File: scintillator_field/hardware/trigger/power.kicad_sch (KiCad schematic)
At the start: 16 parts, among them U2 TPS7A4701, U4 TPS7A4701, U5 LT3461A

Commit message: conclude schematic
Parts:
- added R10: 12k 0.1%, symbol Device:R
- added R9: 10k 0.1%, symbol Device:R
- C1: renamed from C16; footprint (none) -> Capacitor_SMD:C_0402_1005Metric
- C2: renamed from C17; footprint (none) -> Capacitor_SMD:C_0402_1005Metric
- C3: renamed from C15; footprint (none) -> Capacitor_SMD:C_0402_1005Metric
- C4: renamed from C1; footprint (none) -> Capacitor_SMD:C_0402_1005Metric
- C5: renamed from C18; value 47u -> 10u; footprint (none) -> Capacitor_SMD:C_1206_3216Metric
- C6: renamed from C19; footprint (none) -> Capacitor_SMD:C_0402_1005Metric
- C7: renamed from C20; value 47u -> 10u; footprint (none) -> Capacitor_SMD:C_1206_3216Metric
- C8: renamed from C14; footprint (none) -> Capacitor_SMD:C_0402_1005Metric
- renumbered R4 to R5, R2 to R6, R6 to R7, R7 to R8, U5 to U1, U4 to U3
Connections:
- net +3.8V: now also R9.1
- net GND: now also R10.1
- new net +2.1V: R10.2, R9.2
- no-connect marks 0 -> 14
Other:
- moved on the sheet: C1, C2, C3, C4, C5, C6, C7, C8, L1, R5, R6, R7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

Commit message: pcb v1
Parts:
- added C45: 1u, Capacitor_SMD:C_0402_1005Metric, symbol Device:C
- added C46: 0.1u, Capacitor_SMD:C_0402_1005Metric, symbol Device:C
- L1: footprint (none) -> lqh3npn:L_Murata_LQH3NPN_3.0x3.0mm
- R10, R5: footprint (none) -> Resistor_SMD:R_0402_1005Metric
- R6, R7, R8, R9: footprint (none) -> Resistor_SMD:R_0603_1608Metric
- U2, U3: symbol Regulator_Linear:TPS7A4701xRGW -> tps7a4701:TPS7A4701xRGW
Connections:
- net +5V: now also C45.1, C46.1
- net GND: now also U2.17 (NC), U2.18 (NC), U2.19 (NC), U2.2 (NC), U3.17 (NC), U3.18 (NC), U3.19 (NC), U3.2 (NC), C45.2, C46.2
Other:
- moved on the sheet: C1, C2, C7, L1, R5, R6, R7, R8, U1

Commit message: pcb fabrication files
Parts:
- C1: LCSC (none) -> C88923
- C2, C3, C4, C45, C6, C8: LCSC (none) -> C52923
- C46: LCSC (none) -> C1581
- C5, C7: LCSC (none) -> C13585
- L1: LCSC (none) -> C237408
- R10, R5: LCSC (none) -> C317927
- R6: LCSC (none) -> C861317
- R7: LCSC (none) -> C861233
- R8, R9: LCSC (none) -> C136139
- U1: LCSC (none) -> C481768
- U2, U3: LCSC (none) -> C90084
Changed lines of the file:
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@@
+			)
+		)
+		(property "LCSC" "C136139"
+			(at 149.86 99.06 0)
+			(effects
+				(font
+					(size 1.27 1.27)
+				)
+				(hide yes)
 			)
 		)
@@
 			)
 		)
+		(property "LCSC" "C88923"
+			(at 52.07 116.84 0)
+			(effects
+				(font
+					(size 1.27 1.27)
+				)
+				(hide yes)
+			)
+		)
 		(pin "2"
 		)
@@
 			)
 		)
+		(property "LCSC" "C481768"
+			(at 52.07 96.52 0)
+			(effects
+				(font
+					(size 1.27 1.27)
+				)
+				(hide yes)
+			)
+		)
 		(pin "1"
 		)
@@
 			)
 		)
+		(property "LCSC" "C317927"
+			(at 35.56 111.76 0)
+			(effects
+				(font
+					(size 1.27 1.27)
+				)
+				(hide yes)
+			)
+		)
 		(pin "2"
 		)
@@
 			)
 		)
+		(property "LCSC" "C52923"
+			(at 217.17 114.3 0)
+			(effects
+				(font
+					(size 1.27 1.27)
+				)
+				(hide yes)
+			)
+		)
 		(pin "2"
 		)
@@
 			)
 		)
+		(property "LCSC" "C317927"
+			(at 243.84 107.95 0)
+			(effects
+				(font
+					(size 1.27 1.27)
+				)
+				(hide yes)
+			)
+		)
 		(pin "2"
 		)
@@
 			)
 		)
+		(property "LCSC" "C237408"
+			(at 52.07 80.01 0)
+			(effects
+				(font
+					(size 1.27 1.27)
+				)
+				(hide yes)
+			)
+		)
 		(pin "1"
 		)
@@
 			)
 		)
+		(property "LCSC" "C1581"
+			(at 71.12 107.95 0)
+			(effects
+				(font
+					(size 1.27 1.27)
+				)
+				(hide yes)
+			)
+		)
 		(pin "2"
 		)
@@
 		)
 		(property "Description" "Unpolarized capacitor"
+			(at 76.2 107.95 0)
+			(effects
+				(font
+					(size 1.27 1.27)
+				)
+				(hide yes)
+			)
+		)
+		(property "LCSC" "C52923"
 			(at 76.2 107.95 0)
 			(effects
@@
 			)
 		)
+		(property "LCSC" "C52923"
+			(at 110.49 88.9 0)
+			(effects
+				(font
+					(size 1.27 1.27)
+				)
+				(hide yes)
+			)
+		)
 		(pin "2"
 		)
@@
 			)
 		)
+		(property "LCSC" "C90084"
+			(at 203.2 99.06 0)
+			(effects
+				(font
+					(size 1.27 1.27)
+				)
+				(hide yes)
+			)
+		)
 		(pin "5"
 		)
@@
 			)
 		)
+		(property "LCSC" "C136139"
+			(at 243.84 87.63 0)
+			(effects
+				(font
+					(size 1.27 1.27)
+				)
+				(hide yes)
+			)
+		)
 		(pin "1"
 		)
@@
 		)
 		(property "Description" "Unpolarized capacitor"
+			(at 139.7 114.3 0)
+			(effects
+				(font
+					(size 1.27 1.27)
+				)
+				(hide yes)
+			)
+		)
+		(property "LCSC" "C52923"
 			(at 139.7 114.3 0)
 			(effects
@@
 			)
 		)
+		(property "LCSC" "C52923"
+			(at 186.69 90.17 0)
+			(effects
+				(font
+					(size 1.27 1.27)
+				)
+				(hide yes)
+			)
+		)
 		(pin "2"
 		)
@@
 			)
 		)
+		(property "LCSC" "C13585"
+			(at 163.83 93.98 0)
+			(effects
+				(font
+					(size 1.27 1.27)
+				)
+				(hide yes)
+			)
+		)
 		(pin "1"
 		)
@@
 			)
 		)
+		(property "LCSC" "C52923"
+			(at 85.09 107.95 0)
+			(effects
+				(font
+					(size 1.27 1.27)
+				)
+				(hide yes)
+			)
+		)
 		(pin "2"
 		)
@@
 			)
 		)
+		(property "LCSC" "C861317"
+			(at 52.07 111.76 0)
+			(effects
+				(font
+					(size 1.27 1.27)
+				)
+				(hide yes)
+			)
+		)
 		(pin "1"
 		)
@@
 			)
 		)
+		(property "LCSC" "C90084"
+			(at 127 99.06 0)
+			(effects
+				(font
+					(size 1.27 1.27)
+				)
+				(hide yes)
+			)
+		)
 		(pin "5"
 		)
@@
 			)
 		)
+		(property "LCSC" "C861233"
+			(at 149.86 88.9 0)
+			(effects
+				(font
+					(size 1.27 1.27)
+				)
+				(hide yes)
+			)
+		)
 		(pin "1"
 		)
@@
 			(at 227.33 95.25 0)
 			(effects
+				(font
+					(size 1.27 1.27)
+				)
+				(hide yes)
+			)
+		)
+		(property "LCSC" "C13585"
+			(at 227.33 95.25 0)
+			(effects

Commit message: fix trigger pcb
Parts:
- C1: value 1.6p -> 22p; LCSC C88923 -> C70464
- C2, C3, C4, C45, C6, C8: footprint Capacitor_SMD:C_0402_1005Metric -> Capacitor_SMD:C_0603_1608Metric; LCSC C52923 -> C15849
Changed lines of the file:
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@@
 			)
 		)
-		(property "Value" "1.6p"
+		(property "Value" "22p"
 			(at 52.07 123.444 90)
 			(effects
@@
 			)
 		)
-		(property "LCSC" "C88923"
+		(property "LCSC" "C70464"
 			(at 52.07 116.84 0)
 			(effects
@@
 			)
 		)
-		(property "Footprint" "Capacitor_SMD:C_0402_1005Metric"
+		(property "Footprint" "Capacitor_SMD:C_0603_1608Metric"
 			(at 218.1352 118.11 0)
 			(effects
@@
 			)
 		)
-		(property "LCSC" "C52923"
+		(property "LCSC" "C15849"
 			(at 217.17 114.3 0)
 			(effects
@@
 			)
 		)
-		(property "Footprint" "Capacitor_SMD:C_0402_1005Metric"
+		(property "Footprint" "Capacitor_SMD:C_0603_1608Metric"
 			(at 77.1652 111.76 0)
 			(effects
@@
 			)
 		)
-		(property "LCSC" "C52923"
+		(property "LCSC" "C15849"
 			(at 76.2 107.95 0)
 			(effects
@@
 			)
 		)
-		(property "Footprint" "Capacitor_SMD:C_0402_1005Metric"
+		(property "Footprint" "Capacitor_SMD:C_0603_1608Metric"
 			(at 109.5248 92.71 0)
 			(effects
@@
 			)
 		)
-		(property "LCSC" "C52923"
+		(property "LCSC" "C15849"
 			(at 110.49 88.9 0)
 			(effects
@@
 			)
 		)
-		(property "Footprint" "Capacitor_SMD:C_0402_1005Metric"
+		(property "Footprint" "Capacitor_SMD:C_0603_1608Metric"
 			(at 140.6652 118.11 0)
 			(effects
@@
 			)
 		)
-		(property "LCSC" "C52923"
+		(property "LCSC" "C15849"
 			(at 139.7 114.3 0)
 			(effects
@@
 			)
 		)
-		(property "Footprint" "Capacitor_SMD:C_0402_1005Metric"
+		(property "Footprint" "Capacitor_SMD:C_0603_1608Metric"
 			(at 185.7248 93.98 0)
 			(effects
@@
 			)
 		)
-		(property "LCSC" "C52923"
+		(property "LCSC" "C15849"
 			(at 186.69 90.17 0)
 			(effects
@@
 			)
 		)
-		(property "Footprint" "Capacitor_SMD:C_0402_1005Metric"
+		(property "Footprint" "Capacitor_SMD:C_0603_1608Metric"
 			(at 86.0552 111.76 0)
 			(effects
@@
 			)
 		)
-		(property "LCSC" "C52923"
+		(property "LCSC" "C15849"
 			(at 85.09 107.95 0)
 			(effects

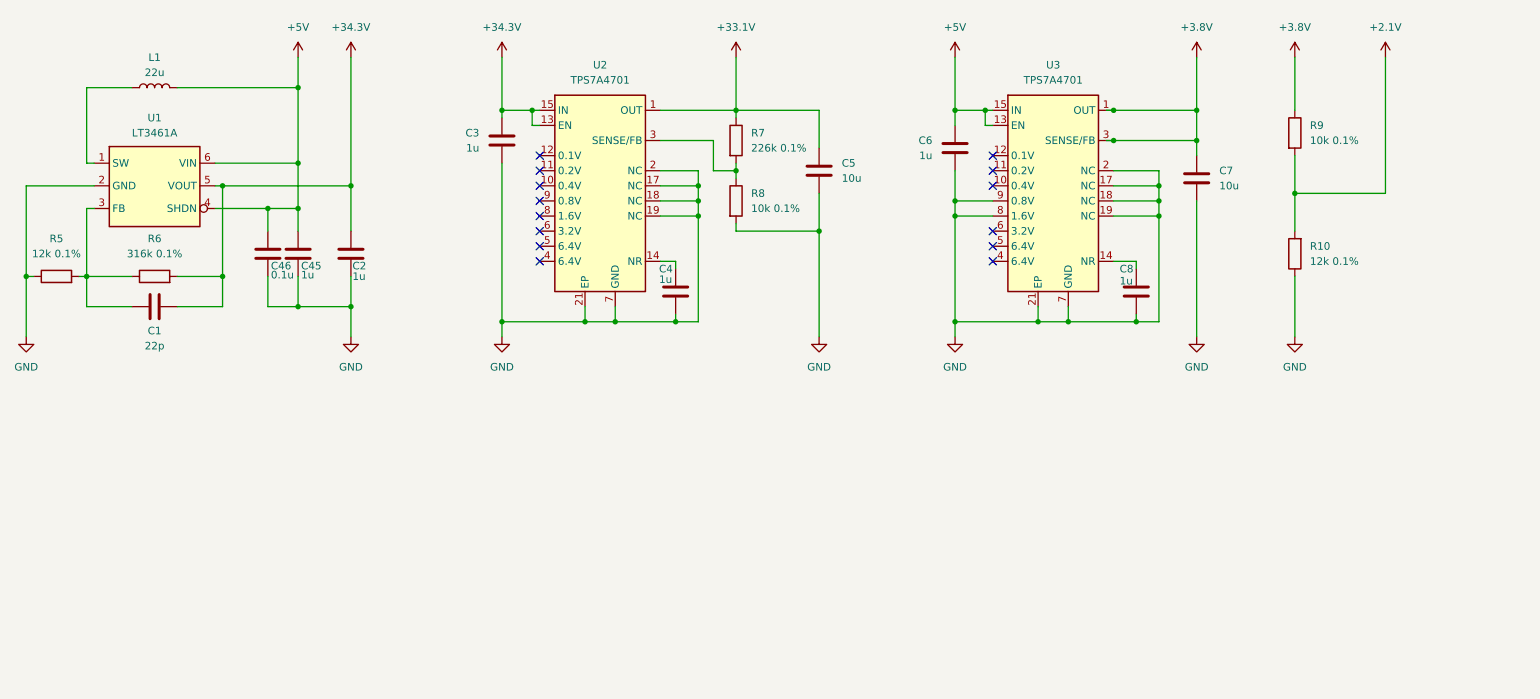
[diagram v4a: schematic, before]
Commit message: update to opa858
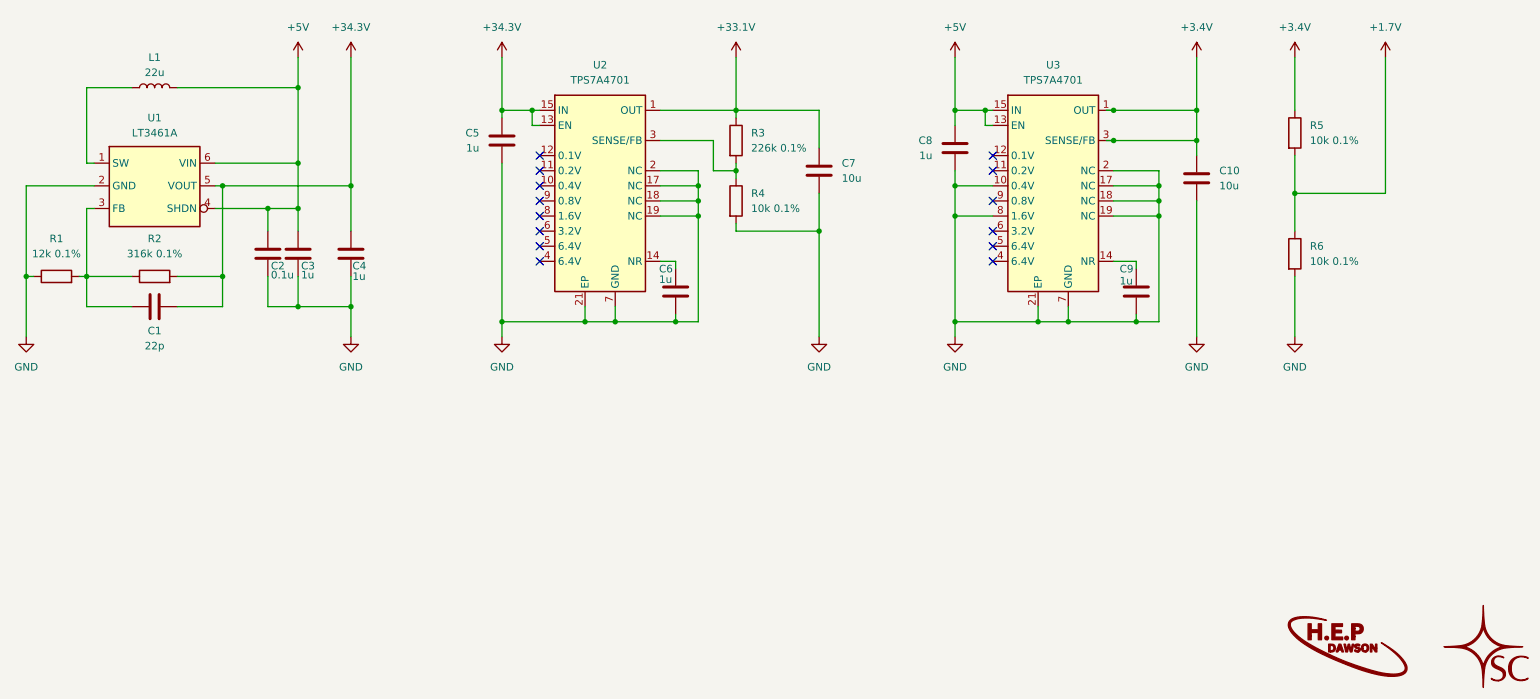
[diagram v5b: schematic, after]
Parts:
- removed R10: 12k 0.1%, Resistor_SMD:R_0402_1005Metric, symbol Device:R
- added R6: 10k 0.1%, Resistor_SMD:R_0603_1608Metric, symbol Device:R
- renumbered C7 to C10, C46 to C2, C45 to C3, C2 to C4, C3 to C5, C4 to C6, C5 to C7, C6 to C8, C8 to C9, R5 to R1, R6 to R2, R7 to R3, R8 to R4, R9 to R5
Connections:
- net GND: now also U3.10 (0.4V), R6.2; no longer U3.9 (0.8V)
- net +2.1V renamed +1.7V
- net +1.7V: now also R6.1
- net +3.8V renamed +3.4V
